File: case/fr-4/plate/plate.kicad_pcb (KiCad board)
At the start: 2 copper layers, 152.4 x 104.6 mm, 33 parts

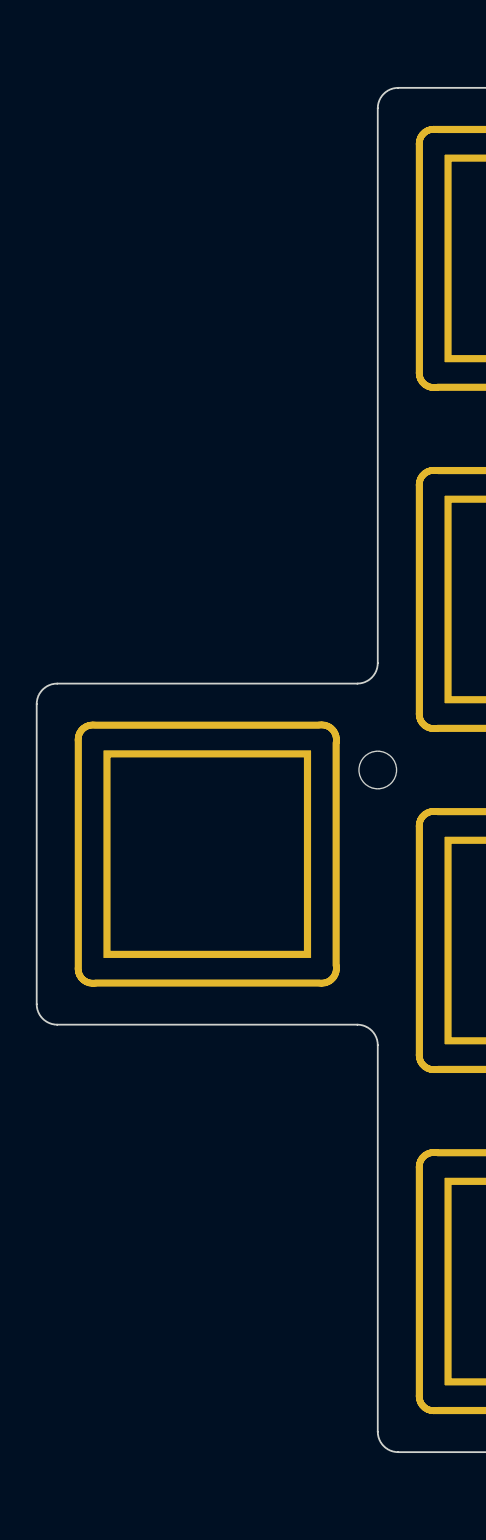
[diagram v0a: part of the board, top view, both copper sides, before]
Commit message: Create cutoff for pinky key
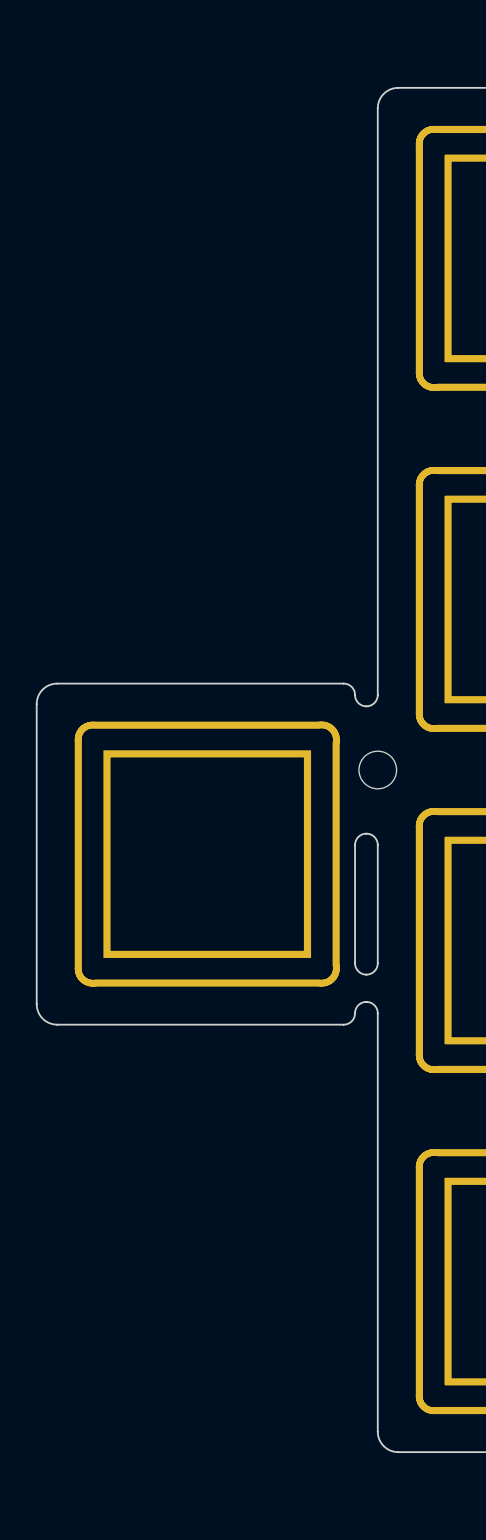
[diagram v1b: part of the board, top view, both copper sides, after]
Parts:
- added REF**: Hole_Mount_M4, jiran-ble-lite:Hole_Mount_M4, F.Cu at (89.0, 101.0)
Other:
- outline, holes or cut-outs redrawn

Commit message: Fill all zones
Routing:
- added copper zone on B.Cu, net (none)
- added copper zone on F.Cu, net (none)
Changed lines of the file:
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@@
   (gr_arc (start 88.392 105.156) (end 87.757004 105.156) (angle 90) (layer "Edge.Cuts") (width 0.1))
   (gr_line (start 203.327 56.896) (end 203.327 133.096) (layer "Edge.Cuts") (width 0.1))
+  (zone (net 0) (net_name "") (layer "F.Cu") (hatch edge 0.508)
+    (connect_pads (clearance 0.508))
+    (min_thickness 0.254) (filled_areas_thickness no)
+    (fill yes (thermal_gap 0.508) (thermal_bridge_width 0.508))
+    (polygon
+      (pts
+        (xy 165.227 53.467)
+        (xy 184.277 53.467)
+        (xy 184.277 55.753)
+        (xy 203.327 55.753)
+        (xy 203.327 134.239)
+        (xy 222.377 134.239)
+        (xy 222.377 153.289)
+        (xy 203.327 153.289)
+        (xy 203.327 151.003)
+        (xy 184.277 151.003)
+        (xy 184.277 148.717)
+        (xy 165.227 148.717)
+        (xy 165.227 124.841)
+        (xy 146.177 124.841)
+        (xy 146.177 129.667)
+        (xy 127.127 129.667)
+        (xy 127.127 136.779)
+        (xy 108.077 136.779)
+        (xy 108.077 139.065)
+        (xy 89.027 139.065)
+        (xy 89.027 115.189)
+        (xy 69.977 115.189)
+        (xy 69.977 96.139)
+        (xy 89.027 96.139)
+        (xy 89.027 62.865)
+        (xy 108.077 62.865)
+        (xy 108.077 60.579)
+        (xy 127.127 60.579)
+        (xy 127.127 53.467)
+        (xy 146.177 53.467)
+        (xy 146.177 48.641)
+        (xy 165.227 48.641)
+      )
+    )
+  )
+  (zone (net 0) (net_name "") (layer "B.Cu") (hatch edge 0.508)
+    (connect_pads (clearance 0.508))
+    (min_thickness 0.254) (filled_areas_thickness no)
+    (fill yes (thermal_gap 0.508) (thermal_bridge_width 0.508))
+    (polygon
+      (pts
+        (xy 165.227 53.467)
+        (xy 184.277 53.467)
+        (xy 184.277 55.753)
+        (xy 203.327 55.753)
+        (xy 203.327 134.239)
+        (xy 222.377 134.239)
+        (xy 222.377 153.289)
+        (xy 203.327 153.289)
+        (xy 203.327 151.003)
+        (xy 184.277 151.003)
+        (xy 184.277 148.717)
+        (xy 165.227 148.717)
+        (xy 165.227 124.841)
+        (xy 146.177 124.841)
+        (xy 146.177 129.667)
+        (xy 127.127 129.667)
+        (xy 127.127 136.779)
+        (xy 108.077 136.779)
+        (xy 108.077 139.065)
+        (xy 89.027 139.065)
+        (xy 89.027 115.189)
+        (xy 69.977 115.189)
+        (xy 69.977 96.139)
+        (xy 89.027 96.139)
+        (xy 89.027 62.865)
+        (xy 108.077 62.865)
+        (xy 108.077 60.579)
+        (xy 127.127 60.579)
+        (xy 127.127 53.467)
+        (xy 146.177 53.467)
+        (xy 146.177 48.641)
+        (xy 165.227 48.641)
+      )
+    )
+  )
 )
